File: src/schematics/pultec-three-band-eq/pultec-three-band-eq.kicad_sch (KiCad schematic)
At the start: 55 parts, among them J1 IN, J10 Low Boost Select Return, J11 Low Boost Level, J12 Hi Cut Select Return, J13 Frequency Selector Send, J19 Inductor Return, J2 OUT, J20 Boost High Q, J21 Boost High, J22 100mH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

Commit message: - fixed unrouted traces
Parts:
- J10: value Low Boost Select Return -> Lo Boost Sel Ret
- J11: value Low Boost Level -> Lo Boost Lvl
- J12: value Hi Cut Select Return -> Hi Cut Sel Ret
- J13: value Frequency Selector Send -> Hi Boost Sel Snd
- J19: value Inductor Return -> Hi Boost Sel Ret
- J20: value Boost High Q -> Hi Boost Q
- J21: value Boost High -> Hi Boost Lvl
- J3: value Hi Cut Select Send -> Hi Cut Sel Snd
- J4: value HI CUT -> Hi Cut Lvl
- J5: value Low Cut Select Send -> Lo Cut Sel Snd
- J6: value Low Boost Select Send -> Lo Boost Sel Snd
- J7: value Low Cut Level -> Low Cut Lvl
- J8: value High Boost Selector Return -> Hi Boost Sel Rtn
- J9: value Low Cut Select Return -> Low Cut Sel Ret
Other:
- added sheet pultec-mid-band (pultec-mid-band.kicad_sch)
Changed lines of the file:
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@@
 		)
 	)
-	(text_box "High Cut"
+	(text_box "High Cut Level"
 		(exclude_from_sim no)
 		(at 177.292 91.694 0)
@@
 			)
 		)
-		(property "Value" "Hi Cut Select Return"
+		(property "Value" "Hi Cut Sel Ret"
 			(at 250.698 149.86 0)
 			(effects
@@
 			)
 		)
-		(property "Value" "Low Cut Select Send"
+		(property "Value" "Lo Cut Sel Snd"
 			(at 146.05 72.644 0)
 			(effects
@@
 			)
 		)
-		(property "Value" "Low Boost Select Send"
+		(property "Value" "Lo Boost Sel Snd"
 			(at 234.696 36.322 0)
 			(effects
@@
 			)
 		)
-		(property "Value" "Boost High"
+		(property "Value" "Hi Boost Lvl"
 			(at 64.77 134.6201 90)
 			(effects
@@
 			)
 		)
-		(property "Value" "Low Boost Level"
+		(property "Value" "Lo Boost Lvl"
 			(at 201.93 26.67 0)
 			(effects
@@
 		(on_board yes)
 		(dnp no)
-		(fields_autoplaced yes)
 		(property "Reference" "J4"
 			(at 271.78 96.5199 0)
@@
 			)
 		)
-		(property "Value" "HI CUT"
-			(at 271.78 99.0599 0)
+		(property "Value" "Hi Cut Lvl"
+			(at 266.192 103.378 0)
 			(effects
 				(font
@@
 			)
 		)
-		(property "Value" "Low Cut Select Return"
+		(property "Value" "Low Cut Sel Ret"
 			(at 162.56 41.402 0)
 			(effects
@@
 			)
 		)
-		(property "Value" "Hi Cut Select Send"
+		(property "Value" "Hi Cut Sel Snd"
 			(at 256.032 118.618 0)
 			(effects
@@
 			)
 		)
-		(property "Value" "Frequency Selector Send"
+		(property "Value" "Hi Boost Sel Snd"
 			(at 24.638 144.018 0)
 			(effects
@@
 			)
 		)
-		(property "Value" "High Boost Selector Return"
+		(property "Value" "Hi Boost Sel Rtn"
 			(at 153.416 150.114 0)
 			(effects
@@
 			)
 		)
-		(property "Value" "Low Cut Level"
+		(property "Value" "Low Cut Lvl"
 			(at 110.49 34.2899 0)
 			(effects
@@
 			)
 		)
-		(property "Value" "Low Boost Select Return"
+		(property "Value" "Lo Boost Sel Ret"
 			(at 230.124 72.136 0)
 			(effects
@@
 			)
 		)
-		(property "Value" "Inductor Return"
+		(property "Value" "Hi Boost Sel Ret"
 			(at 36.83 118.11 0)
 			(effects
@@
 			)
 		)
-		(property "Value" "Boost High Q"
+		(property "Value" "Hi  Boost Q"
 			(at 62.23 118.1099 90)
 			(effects
@@
 				)
 			)
+		)
+	)
+	(sheet
+		(at 19.304 165.862)
+		(size 34.29 19.558)
+		(fields_autoplaced yes)
+		(stroke
+			(width 0.1524)
+			(type solid)
+		)
+		(fill
+			(color 0 0 0 0.0000)
+		)
+		(property "Sheetname" "pultec-mid-band"
+			(at 19.304 165.1504 0)
+			(effects
+				(font
+					(size 1.27 1.27)
+				)
+				(justify left bottom)
+			)
+		)
+		(property "Sheetfile" "pultec-mid-band.kicad_sch"
+			(at 19.304 186.0046 0)
+			(effects
+				(font
+					(size 1.27 1.27)
+				)
+				(justify left top)
+			)
+		)
+		(instances
+			(project "pultec-three-band-eq"
+				(path "/70789860-d793-449c-9aa5-cfb021a8ba37"
+					(page "2")
+				)
+			)

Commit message: - fixed issue with hierarchical label - fixed unrouted trace related to issue with hierarchical label - Updated PCB identifier in front copper and front fab layers to use variables instead of hard-coded dates and revisions.
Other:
- sheet pultec-mid-band ports: added HI BOOST OUT H; removed none
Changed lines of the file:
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@@
 	)
 	(junction
+		(at 102.87 68.58)
+		(diameter 0)
+		(color 0 0 0 0)
+	)
+	(junction
 		(at 189.23 140.97)
 		(diameter 0)
@@
 	(wire
 		(pts
-			(xy 62.23 127) (xy 62.23 130.81)
+			(xy 224.79 130.81) (xy 232.41 130.81)
 		)
 		(stroke
@@
 	(wire
 		(pts
-			(xy 224.79 130.81) (xy 232.41 130.81)
+			(xy 208.28 68.58) (xy 247.65 68.58)
 		)
 		(stroke
@@
 	(wire
 		(pts
-			(xy 208.28 68.58) (xy 247.65 68.58)
+			(xy 246.38 55.88) (xy 247.65 55.88)
 		)
 		(stroke
@@
 	(wire
 		(pts
-			(xy 246.38 55.88) (xy 247.65 55.88)
+			(xy 232.41 130.81) (xy 232.41 133.35)
 		)
 		(stroke
@@
 	(wire
 		(pts
-			(xy 232.41 130.81) (xy 232.41 133.35)
+			(xy 15.24 90.17) (xy 102.87 90.17)
 		)
 		(stroke
@@
 	(wire
 		(pts
-			(xy 102.87 66.04) (xy 102.87 68.58)
-		)
-		(stroke
-			(width 0)
-			(type default)
-		)
-	)
-	(wire
-		(pts
 			(xy 25.4 137.16) (xy 31.75 137.16)
 		)
@@
 	(wire
 		(pts
+			(xy 102.87 66.04) (xy 102.87 68.58)
+		)
+		(stroke
+			(width 0)
+			(type default)
+		)
+	)
+	(wire
+		(pts
 			(xy 179.07 146.05) (xy 179.07 154.94)
 		)
@@
 	(wire
 		(pts
+			(xy 15.24 90.17) (xy 15.24 177.8)
+		)
+		(stroke
+			(width 0)
+			(type default)
+		)
+	)
+	(wire
+		(pts
 			(xy 200.66 55.88) (xy 200.66 58.42)
 		)
@@
 	(wire
 		(pts
+			(xy 15.24 177.8) (xy 19.304 177.8)
+		)
+		(stroke
+			(width 0)
+			(type default)
+		)
+	)
+	(wire
+		(pts
 			(xy 189.23 130.81) (xy 207.01 130.81)
 		)
@@
 	(wire
 		(pts
+			(xy 62.23 127) (xy 62.23 130.81)
+		)
+		(stroke
+			(width 0)
+			(type default)
+		)
+	)
+	(wire
+		(pts
 			(xy 238.76 55.88) (xy 200.66 55.88)
 		)
@@
 	(wire
 		(pts
+			(xy 102.87 68.58) (xy 102.87 90.17)
+		)
+		(stroke
+			(width 0)
+			(type default)
+		)
+	)
+	(wire
+		(pts
 			(xy 232.41 133.35) (xy 232.41 135.89)
 		)
@@
 			)
 		)
+		(pin "HI BOOST OUT H" input
+			(at 19.304 177.8 180)
+			(effects
+				(font
+					(size 1.27 1.27)
+				)
+				(justify left)
+			)
+		)

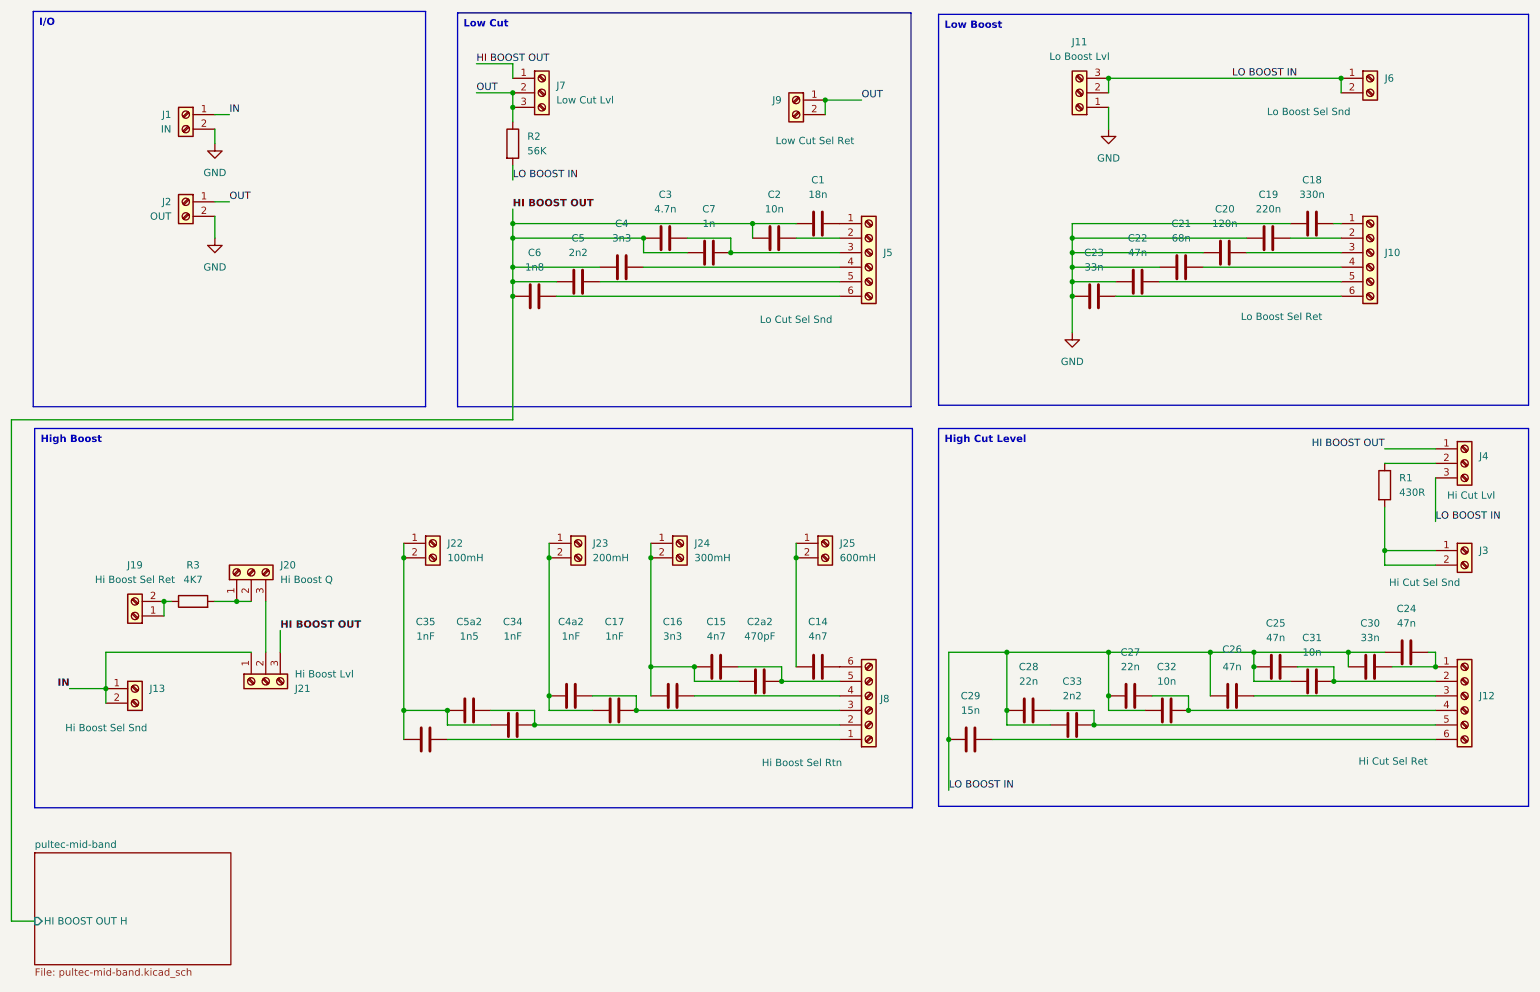
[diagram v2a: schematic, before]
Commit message: - re-worked the mid-range - exported gerbers for PCB manufacture
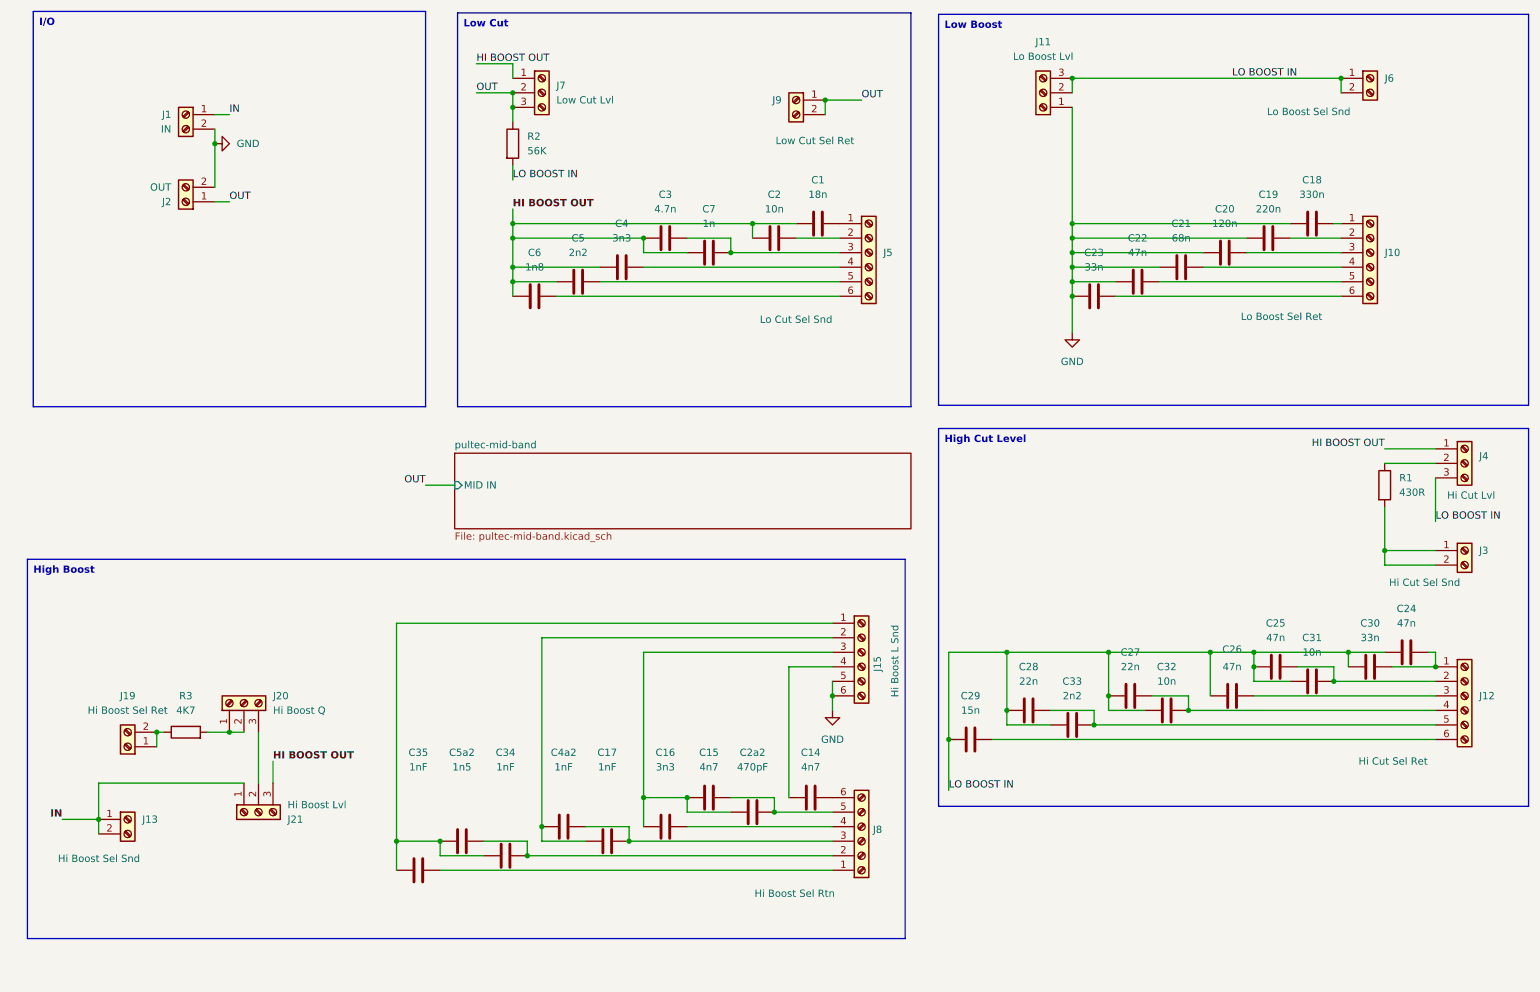
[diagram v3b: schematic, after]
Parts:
- removed J22: 100mH, OL Library:TerminalBlock_Phoenix_MKDS-1,5-2_1x02_P5.00mm_Horizontal Fat Pad, symbol Connector:Screw_Terminal_01x02
- removed J23: 200mH, OL Library:TerminalBlock_Phoenix_MKDS-1,5-2_1x02_P5.00mm_Horizontal Fat Pad, symbol Connector:Screw_Terminal_01x02
- removed J24: 300mH, OL Library:TerminalBlock_Phoenix_MKDS-1,5-2_1x02_P5.00mm_Horizontal Fat Pad, symbol Connector:Screw_Terminal_01x02
- removed J25: 600mH, OL Library:TerminalBlock_Phoenix_MKDS-1,5-2_1x02_P5.00mm_Horizontal Fat Pad, symbol Connector:Screw_Terminal_01x02
- added J15: Hi Boost L Snd, TerminalBlock_Phoenix:TerminalBlock_Phoenix_MKDS-1,5-6_1x06_P5.00mm_Horizontal, symbol Connector:Screw_Terminal_01x06
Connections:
- net GND: now also J15.5 (Pin_5), J15.6 (Pin_6)
- net at C14.1: now also J15.4 (Pin_4)
- net at C34.1, C35.1, C5a2.1: now also J15.1 (Pin_1)
- net at C15.1, C16.1, C2a2.1: now also J15.3 (Pin_3)
- net at C17.1, C4a2.1: now also J15.2 (Pin_2)
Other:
- sheet pultec-mid-band ports: added MID IN; removed HI BOOST OUT H
- moved on the sheet: C14, C15, C16, C17, C2a2, C34, C35, C4a2, C5a2, J11, J13, J19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
